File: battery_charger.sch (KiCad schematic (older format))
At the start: 20 parts

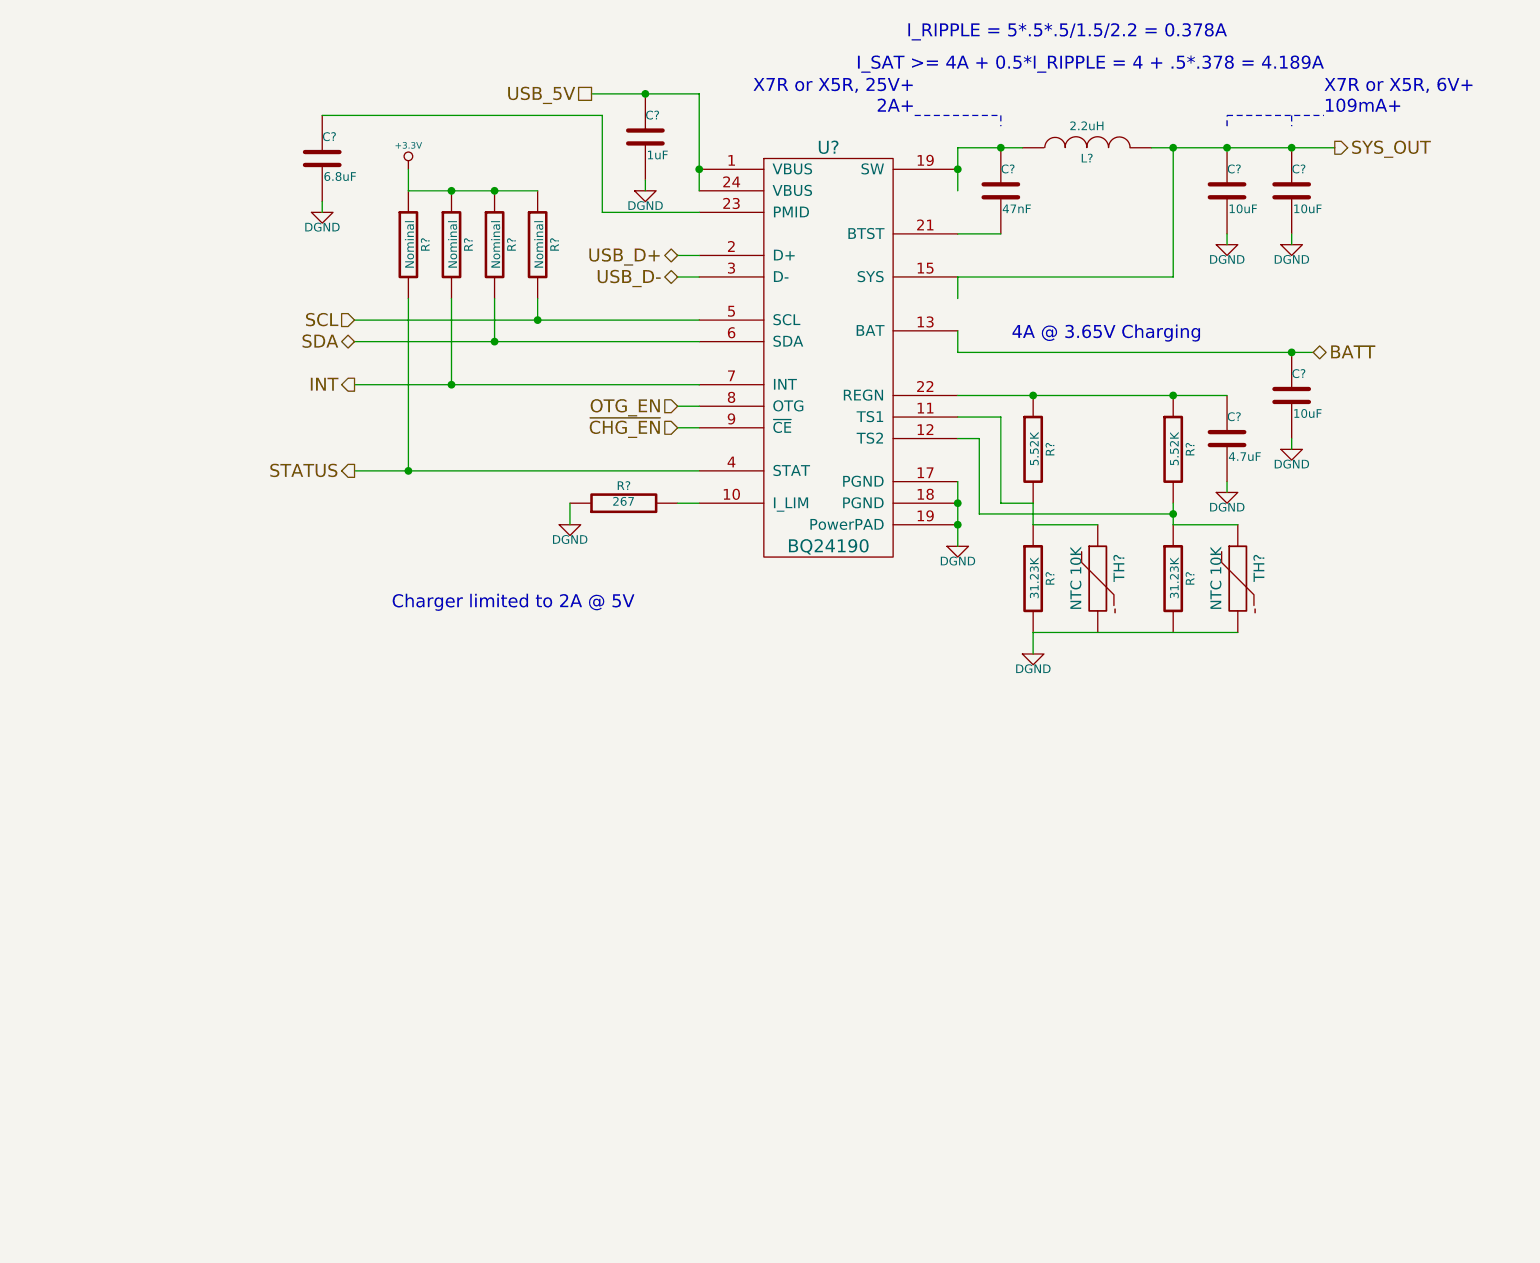
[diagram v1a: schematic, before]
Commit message: added pullups/downs as necessary, added test pts
also added interrupt conn to msp from charger, made led part for generic
indicators, added generic indicators to psu's
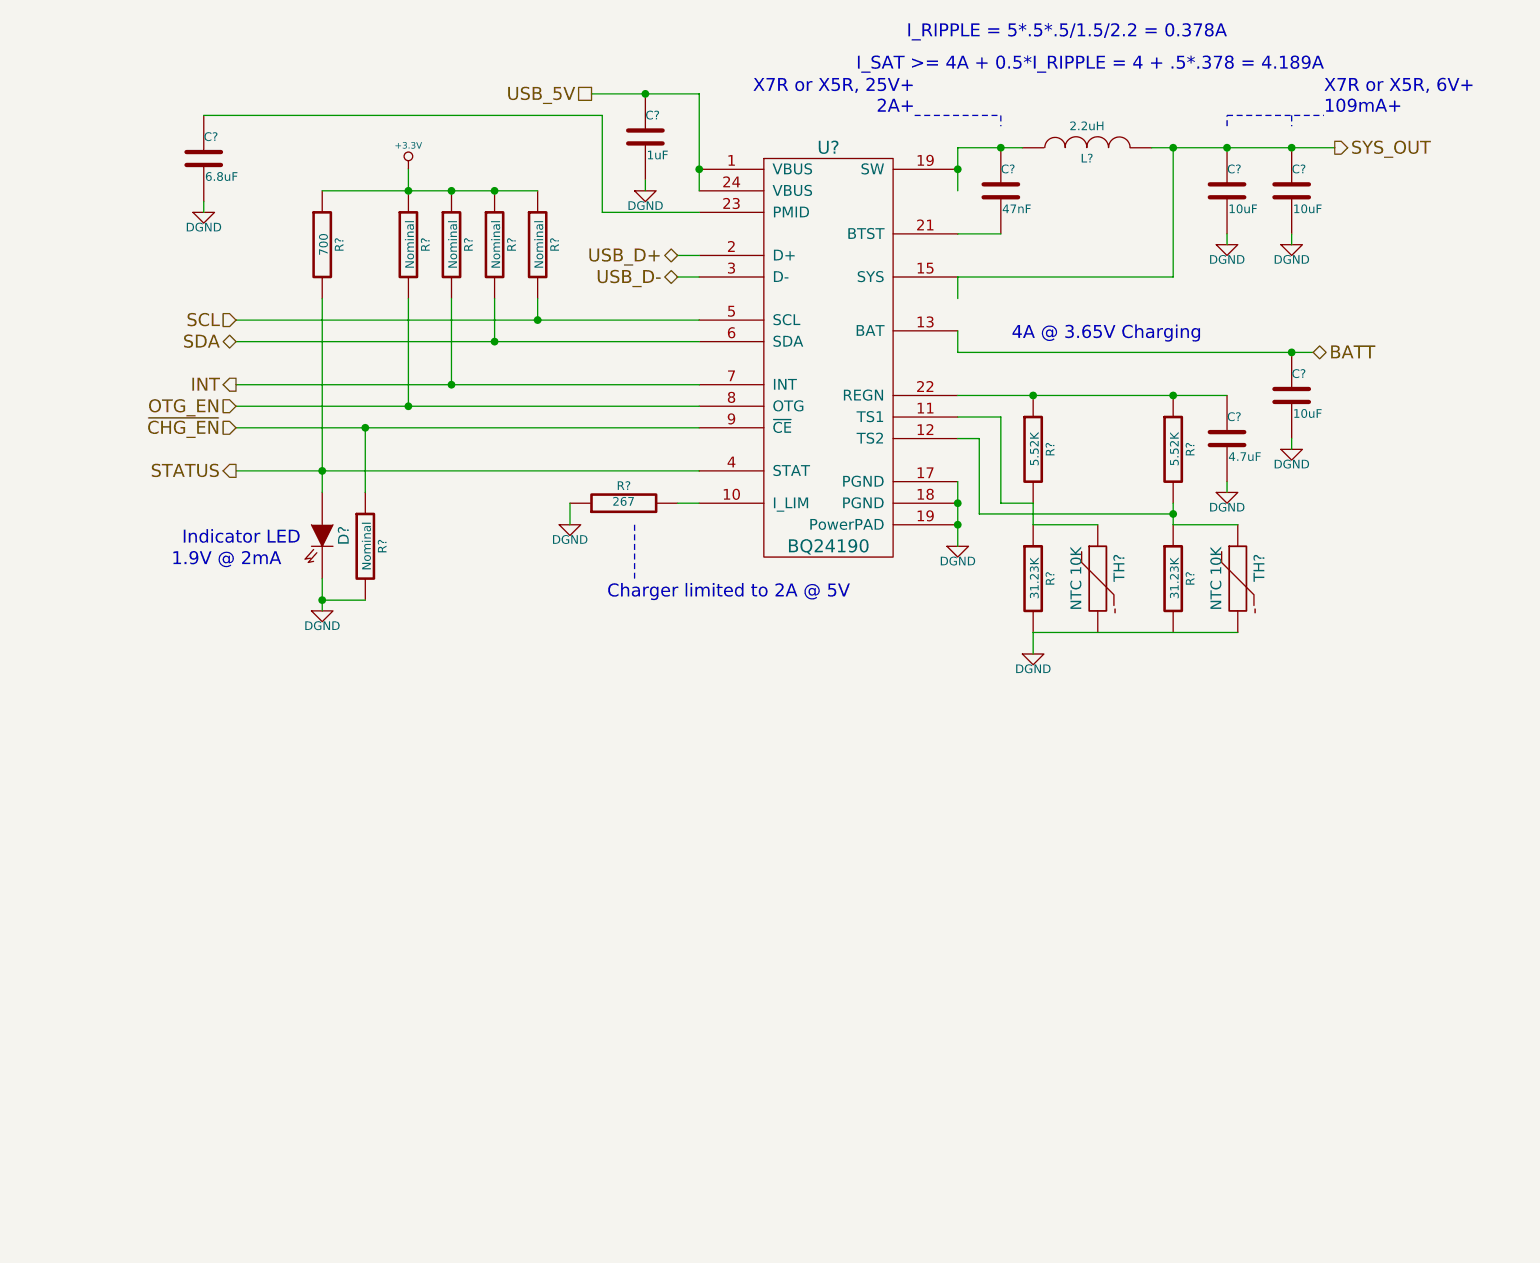
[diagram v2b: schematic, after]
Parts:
- removed R?: Nominal, ~, symbol R
- added D?: LED_GENERIC_SMD, ~, symbol LED_GENERIC_SMD
- added R? (x2): Nominal, ~, symbol R
- added R?: 700, ~, symbol R
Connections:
- wire segments 69 -> 54
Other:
- note added: "1.9V @ 2mA"
- note added: "Indicator LED"
- moved on the sheet: C?
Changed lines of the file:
@@
 $Descr A4 11693 8268
 encoding utf-8
-Sheet 14 18
+Sheet 18 18
 Title ""
-Date "14 dec 2013"
+Date "18 dec 2013"
 Rev ""
 Comp ""
@@
 	0    -1   -1   0
 $EndComp
-Text HLabel 2600 3150 0    60   Output ~ 0
+Text HLabel 2050 3150 0    60   Output ~ 0
 STATUS
 $Comp
@@
 $EndComp
 Wire Wire Line
-	5400 3200 5400 3300
-Wire Wire Line
-	5400 3300 5400 3400
-Wire Wire Line
-	5400 3400 5400 3500
+	5400 3200 5400 3500
 Connection ~ 5400 3300
 Connection ~ 5400 3400
@@
 	3600 3300 3600 3400
 Wire Wire Line
-	5400 2800 5750 2800
-Wire Wire Line
-	5750 2800 6400 2800
-Wire Wire Line
-	6400 2800 6650 2800
+	5400 2800 6650 2800
 Connection ~ 5750 2800
 Wire Wire Line
@@
 	5600 3300 5750 3300
 Wire Wire Line
-	6400 3300 6400 3350
-Wire Wire Line
-	6400 3350 6400 3400
+	6400 3300 6400 3400
 Connection ~ 6400 3350
 Wire Wire Line
@@
 	3450 2350 3450 2450
 Wire Wire Line
-	2600 2450 3450 2450
-Wire Wire Line
-	3450 2450 4200 2450
-Wire Wire Line
-	2600 2550 3250 2550
-Wire Wire Line
-	3250 2550 4200 2550
+	2050 2450 4200 2450
+Wire Wire Line
+	2050 2550 4200 2550
 Wire Wire Line
 	3250 2550 3250 2350
@@
 	3050 2350 3050 2750
 Wire Wire Line
-	2600 2750 3050 2750
-Wire Wire Line
-	3050 2750 4200 2750
-Text HLabel 2600 2450 0    60   Input ~ 0
+	2050 2750 4200 2750
+Text HLabel 2050 2450 0    60   Input ~ 0
 SCL
-Text HLabel 2600 2550 0    60   BiDi ~ 0
+Text HLabel 2050 2550 0    60   BiDi ~ 0
 SDA
-Text HLabel 2600 2750 0    60   Output ~ 0
+Text HLabel 2050 2750 0    60   Output ~ 0
 INT
 Wire Wire Line
@@
 	4100 2250 4200 2250
 Wire Wire Line
-	4200 1400 4200 1750
-Wire Wire Line
-	4200 1750 4200 1850
+	4200 1400 4200 1850
 $Comp
 L C C?
@@
 Connection ~ 4200 1750
 Wire Wire Line
-	3700 1400 3950 1400
-Wire Wire Line
-	3950 1400 4200 1400
+	3700 1400 4200 1400
 Connection ~ 3950 1400
 $Comp
@@
 	3750 1950 3750 1500
 Wire Wire Line
-	3750 1500 2450 1500
+	3750 1500 1900 1500
 $Comp
 L +3.3V #PWR?
@@
 $EndComp
 Wire Wire Line
-	2850 1850 3050 1850
-Wire Wire Line
-	3050 1850 3250 1850
-Wire Wire Line
-	3250 1850 3450 1850
+	2450 1850 3450 1850
 Connection ~ 3250 1850
 $Comp
 L C C?
 U 1 1 52AAD4A2
-P 2450 1700
-F 0 "C?" H 2450 1800 40  0000 L CNN
-F 1 "6.8uF" H 2456 1615 40  0000 L CNN
-F 2 "~" H 2488 1550 30  0000 C CNN
-F 3 "~" H 2450 1700 60  0000 C CNN
-	1    2450 1700
+P 1900 1700
+F 0 "C?" H 1900 1800 40  0000 L CNN
+F 1 "6.8uF" H 1906 1615 40  0000 L CNN
+F 2 "~" H 1938 1550 30  0000 C CNN
+F 3 "~" H 1900 1700 60  0000 C CNN
+	1    1900 1700
 	1    0    0    -1
 $EndComp
@@
 L DGND #PWR?
 U 1 1 52AAD4B3
-P 2450 1950
-F 0 "#PWR?" H 2450 1950 40  0001 C CNN
-F 1 "DGND" H 2450 1880 40  0000 C CNN
-F 2 "" H 2450 1950 60  0000 C CNN
-F 3 "" H 2450 1950 60  0000 C CNN
-	1    2450 1950
-	1    0    0    -1
-$EndComp
-Wire Wire Line
-	2450 1950 2450 1900
-Text HLabel 4100 2850 0    60   Input ~ 0
+P 1900 1950
+F 0 "#PWR?" H 1900 1950 40  0001 C CNN
+F 1 "DGND" H 1900 1880 40  0000 C CNN
+F 2 "" H 1900 1950 60  0000 C CNN
+F 3 "" H 1900 1950 60  0000 C CNN
+	1    1900 1950
+	1    0    0    -1
+$EndComp
+Wire Wire Line
+	1900 1950 1900 1900
+Text HLabel 2050 2850 0    60   Input ~ 0
 OTG_EN
-Text HLabel 4100 2950 0    60   Input ~ 0
+Text HLabel 2050 2950 0    60   Input ~ 0
 ~CHG_EN
 Wire Wire Line
-	4100 2850 4200 2850
-Wire Wire Line
-	4100 2950 4200 2950
+	2050 2850 4200 2850
+Wire Wire Line
+	2050 2950 4200 2950
 Connection ~ 3450 2450
 Connection ~ 3250 2550
 Connection ~ 3050 2750
-$Comp
-L R R?
-U 1 1 52AB2B7E
-P 2850 2100
-F 0 "R?" V 2930 2100 40  0000 C CNN
-F 1 "Nominal" V 2857 2101 40  0000 C CNN
-F 2 "~" V 2780 2100 30  0000 C CNN
-F 3 "~" H 2850 2100 30  0000 C CNN
-	1    2850 2100
-	1    0    0    -1
-$EndComp
 Wire Wire Line
 	2850 1750 2850 1850
 Connection ~ 3050 1850
 Wire Wire Line
-	2600 3150 2850 3150
-Wire Wire Line
-	2850 3150 4200 3150
-Wire Wire Line
-	2850 2350 2850 3150
-Connection ~ 2850 3150
+	2050 3150 4200 3150
 $Comp
 L C C?
@@
 	5400 2500 5400 2600
 Wire Wire Line
-	5400 2600 6950 2600
-Wire Wire Line
-	6950 2600 7050 2600
+	5400 2600 7050 2600
 Text HLabel 7050 2600 2    60   BiDi ~ 0
 BATT
@@
 	5400 2050 5600 2050
 Wire Wire Line
-	5400 1650 5400 1750
-Wire Wire Line
-	5400 1750 5400 1850
-Wire Wire Line
-	5400 1650 5600 1650
-Wire Wire Line
-	5600 1650 5700 1650
+	5400 1650 5400 1850
+Wire Wire Line
+	5400 1650 5700 1650
 Connection ~ 5400 1750
 Connection ~ 5600 1650
@@
 	5400 2350 5400 2250
 Wire Wire Line
-	6300 1650 6400 1650
-Wire Wire Line
-	6400 1650 6650 1650
-Wire Wire Line
-	6650 1650 6950 1650
-Wire Wire Line
-	6950 1650 7150 1650
+	6300 1650 7150 1650
 Wire Wire Line
 	6400 1650 6400 2250
@@
 Text HLabel 7150 1650 2    60   Output ~ 0
 SYS_OUT
-Text Notes 3900 3800 2    60   ~ 0
+Text Notes 4900 3750 2    60   ~ 0
 Charger limited to 2A @ 5V
 Text Notes 7100 1300 2    60   ~ 0
@@
 Text Notes 6650 1150 2    60   ~ 0
 I_RIPPLE = 5*.5*.5/1.5/2.2 = 0.378A
+Text Notes 2350 3500 2    60   ~ 0
+Indicator LED
+$Comp
+L LED_GENERIC_SMD D?
+U 1 1 52B37BFF
+P 2450 3450
+F 0 "D?" H 2450 3550 50  0000 C CNN
+F 1 "LED_GENERIC_SMD" H 2450 3300 50  0001 C CNN
+F 2 "~" H 2450 3450 60  0000 C CNN
+F 3 "~" H 2450 3450 60  0000 C CNN
+	1    2450 3450
+	0    1    1    0
+$EndComp
+Text Notes 1750 3600 0    60   ~ 0
+1.9V @ 2mA
+$Comp
+L DGND #PWR?
+U 1 1 52B37C0F
+P 2450 3800
+F 0 "#PWR?" H 2450 3800 40  0001 C CNN
+F 1 "DGND" H 2450 3730 40  0000 C CNN
+F 2 "" H 2450 3800 60  0000 C CNN
+F 3 "" H 2450 3800 60  0000 C CNN
+	1    2450 3800
+	1    0    0    -1
+$EndComp
+Wire Wire Line
+	2450 3800 2450 3650
+Wire Notes Line
+	3900 3400 3900 3650
+Connection ~ 2850 1850
+$Comp
+L R R?
+U 1 1 52B3B9CF
+P 2850 2100
+F 0 "R?" V 2930 2100 40  0000 C CNN
+F 1 "Nominal" V 2857 2101 40  0000 C CNN
+F 2 "~" V 2780 2100 30  0000 C CNN
+F 3 "~" H 2850 2100 30  0000 C CNN
+	1    2850 2100
+	1    0    0    -1
+$EndComp
+Wire Wire Line
+	2850 2350 2850 2850
+Connection ~ 2850 2850
+$Comp
+L R R?
+U 1 1 52B3BA8E
+P 2450 2100
+F 0 "R?" V 2530 2100 40  0000 C CNN
+F 1 "700" V 2457 2101 40  0000 C CNN
+F 2 "~" V 2380 2100 30  0000 C CNN
+F 3 "~" H 2450 2100 30  0000 C CNN
+	1    2450 2100
+	1    0    0    -1
+$EndComp
+Wire Wire Line
+	2450 2350 2450 3250
+Connection ~ 2450 3150
+Wire Wire Line
+	2650 2950 2650 3250
+Connection ~ 2650 2950
+$Comp
+L R R?
+U 1 1 52B3BBFD
+P 2650 3500
+F 0 "R?" V 2730 3500 40  0000 C CNN
+F 1 "Nominal" V 2657 3501 40  0000 C CNN
+F 2 "~" V 2580 3500 30  0000 C CNN
+F 3 "~" H 2650 3500 30  0000 C CNN
+	1    2650 3500
+	1    0    0    -1
+$EndComp
+Wire Wire Line
+	2450 3750 2650 3750
+Connection ~ 2450 3750
 $EndSCHEMATC
